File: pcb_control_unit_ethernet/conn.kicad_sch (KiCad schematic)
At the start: 18 parts, among them J10 TOF1, J11 RGB, J12 LightBarrier1, J13 LightBarrier2, J14 LightBarrier3, J15 PressureTransducer, J16 CAN, J6 USB STM32, J7 Malibotti, J8 TOF3, J9 TOF2

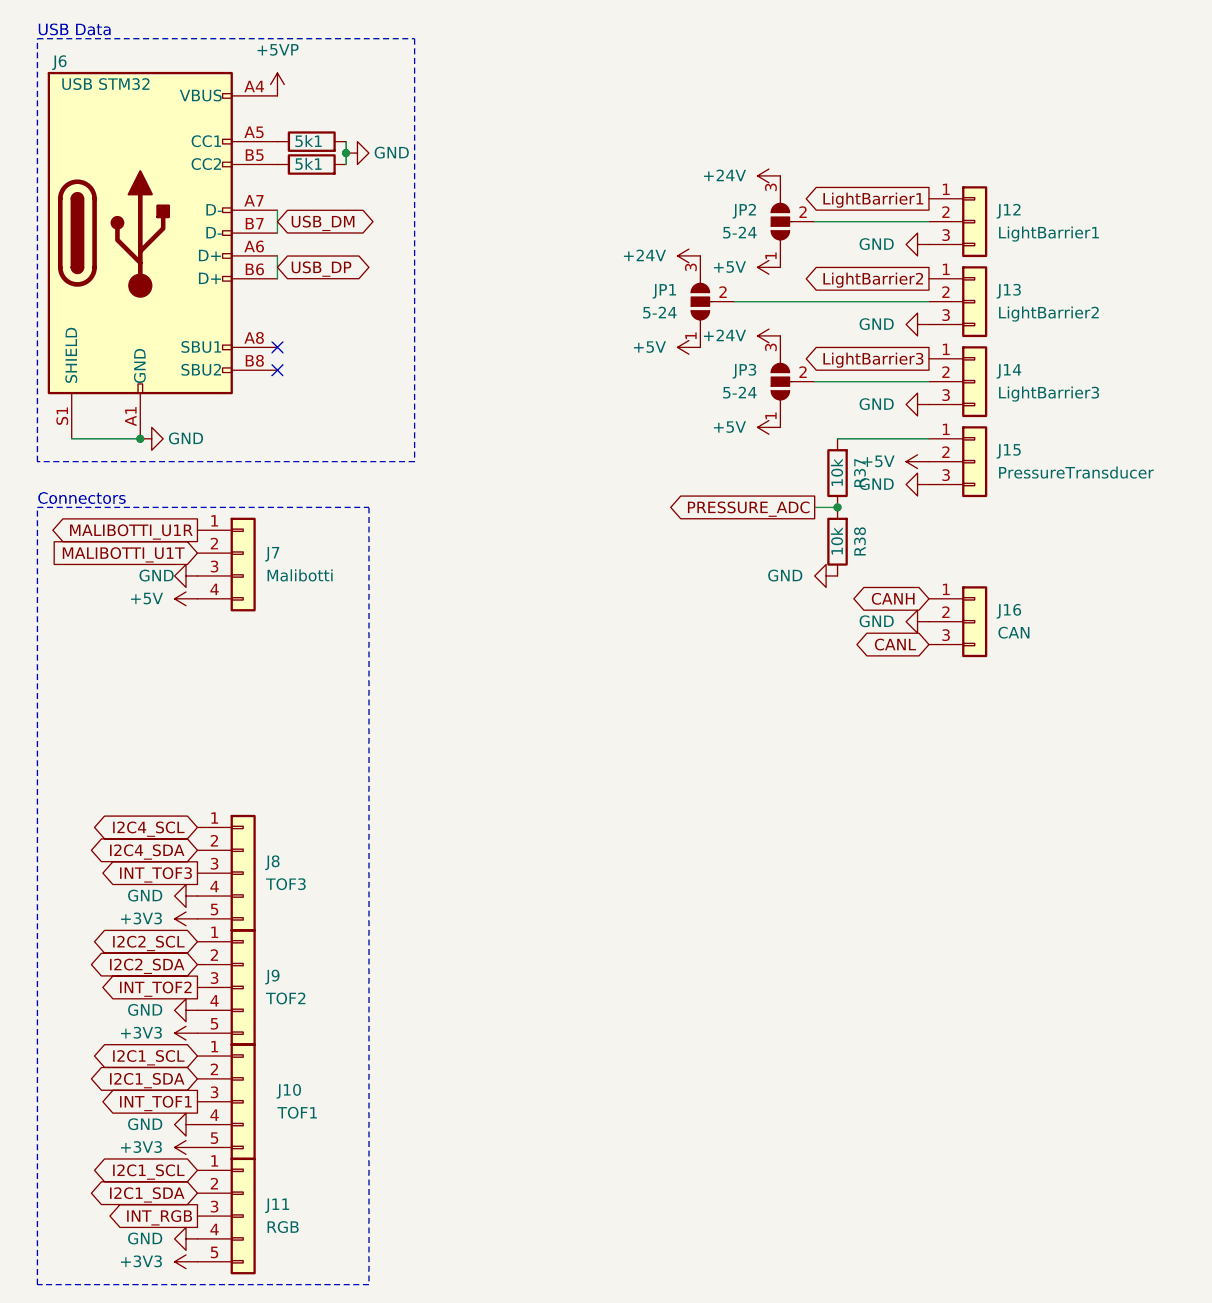
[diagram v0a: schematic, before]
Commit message: First time zero errors, but bad layout
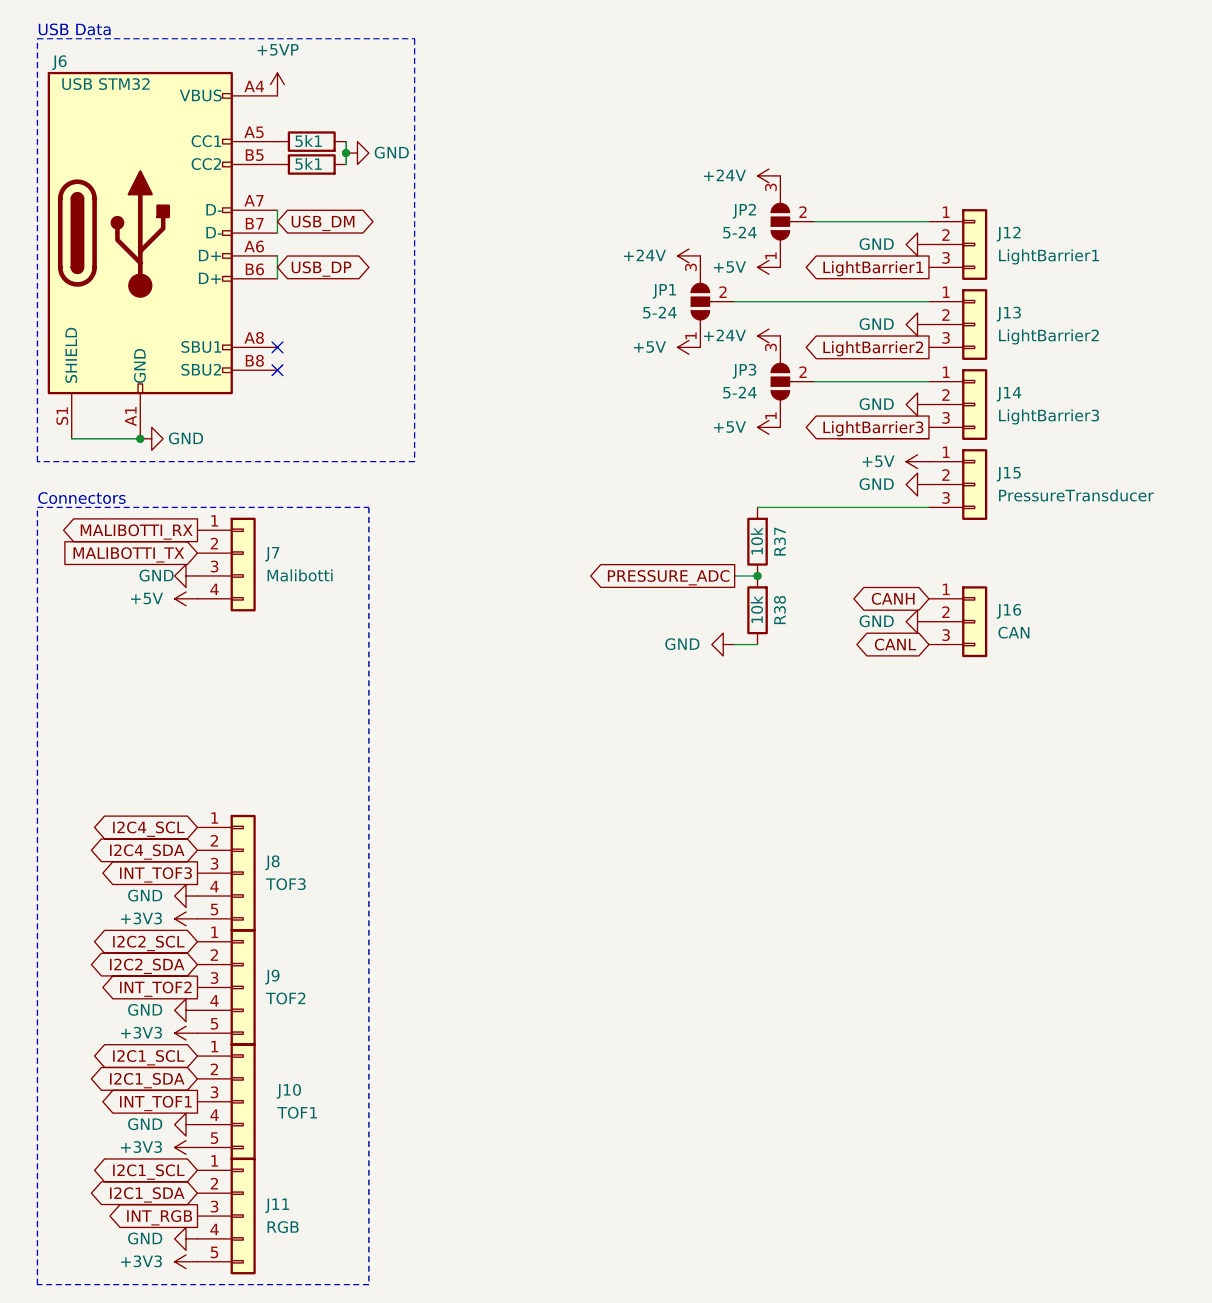
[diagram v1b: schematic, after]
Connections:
- net +5V: now also J15.1 (Pin_1); no longer J15.2 (Pin_2)
- net GND: now also J12.2 (Pin_2), J13.2 (Pin_2), J14.2 (Pin_2), J15.2 (Pin_2); no longer J12.3 (Pin_3), J13.3 (Pin_3), J14.3 (Pin_3), J15.3 (Pin_3)
- net LightBarrier1: now also J12.3 (Pin_3); no longer J12.1 (Pin_1)
- net LightBarrier2: now also J13.3 (Pin_3); no longer J13.1 (Pin_1)
- net LightBarrier3: now also J14.3 (Pin_3); no longer J14.1 (Pin_1)
- net at JP2.2 (C): now also J12.1 (Pin_1); no longer J12.2 (Pin_2)
- net at JP3.2 (C): now also J14.1 (Pin_1); no longer J14.2 (Pin_2)
- net at JP1.2 (C): now also J13.1 (Pin_1); no longer J13.2 (Pin_2)
- net at R37.2: now also J15.3 (Pin_3); no longer J15.1 (Pin_1)
- net MALIBOTTI_U1R renamed MALIBOTTI_RX
- net MALIBOTTI_U1T renamed MALIBOTTI_TX
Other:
- moved on the sheet: J12, J13, J14, J15, R37, R38
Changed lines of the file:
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@@
 	)
 	(junction
-		(at 102.87 67.31)
+		(at 93.98 74.93)
 		(diameter 0)
 		(color 0 0 0 0)
@@
 	(wire
 		(pts
-			(xy 100.33 67.31) (xy 102.87 67.31)
+			(xy 91.44 74.93) (xy 93.98 74.93)
 		)
 		(stroke
@@
 	(wire
 		(pts
+			(xy 91.44 82.55) (xy 93.98 82.55)
+		)
+		(stroke
+			(width 0)
+			(type default)
+		)
+	)
+	(wire
+		(pts
 			(xy 91.44 44.45) (xy 113.03 44.45)
 		)
@@
 		)
 	)
+	(wire
+		(pts
+			(xy 93.98 67.31) (xy 113.03 67.31)
+		)
+		(stroke
+			(width 0)
+			(type default)
+		)
+	)
 	(global_label "INT_TOF2"
 		(shape output)
@@
 	(global_label "LightBarrier3"
 		(shape output)
-		(at 113.03 50.8 180)
+		(at 113.03 58.42 180)
 		(fields_autoplaced yes)
 		(effects
@@
 		)
 		(property "Intersheetrefs" "${INTERSHEET_REFS}"
-			(at 97.7077 50.8 0)
+			(at 97.7077 58.42 0)
 			(effects
 				(font
@@
 		)
 	)
-	(global_label "MALIBOTTI_U1T"
+	(global_label "MALIBOTTI_TX"
 		(shape input)
 		(at 31.75 72.39 180)
@@
 		)
 		(property "Intersheetrefs" "${INTERSHEET_REFS}"
-			(at 14.9762 72.39 0)
+			(at 16.3067 72.39 0)
 			(effects
 				(font
@@
 		)
 	)
-	(global_label "MALIBOTTI_U1R"
+	(global_label "MALIBOTTI_RX"
 		(shape output)
 		(at 31.75 69.85 180)
@@
 		)
 		(property "Intersheetrefs" "${INTERSHEET_REFS}"
-			(at 14.6738 69.85 0)
+			(at 16.0043 69.85 0)
 			(effects
 				(font
@@
 	(global_label "LightBarrier1"
 		(shape output)
-		(at 113.03 33.02 180)
+		(at 113.03 40.64 180)
 		(fields_autoplaced yes)
 		(effects
@@
 		)
 		(property "Intersheetrefs" "${INTERSHEET_REFS}"
-			(at 97.7077 33.02 0)
+			(at 97.7077 40.64 0)
 			(effects
 				(font
@@
 	(global_label "LightBarrier2"
 		(shape output)
-		(at 113.03 41.91 180)
+		(at 113.03 49.53 180)
 		(fields_autoplaced yes)
 		(effects
@@
 		)
 		(property "Intersheetrefs" "${INTERSHEET_REFS}"
-			(at 97.7077 41.91 0)
+			(at 97.7077 49.53 0)
 			(effects
 				(font
@@
 	(global_label "PRESSURE_ADC"
 		(shape output)
-		(at 100.33 67.31 180)
+		(at 91.44 74.93 180)
 		(fields_autoplaced yes)
 		(effects
@@
 		)
 		(property "Intersheetrefs" "${INTERSHEET_REFS}"
-			(at 82.8911 67.31 0)
+			(at 74.0011 74.93 0)
 			(effects
 				(font
@@
 	(symbol
 		(lib_id "Connector_Generic:Conn_01x03")
-		(at 118.11 44.45 0)
+		(at 118.11 46.99 0)
 		(unit 1)
 		(exclude_from_sim no)
@@
 		(fields_autoplaced yes)
 		(property "Reference" "J13"
-			(at 120.65 43.1799 0)
+			(at 120.65 45.7199 0)
 			(effects
 				(font
@@
 		)
 		(property "Value" "LightBarrier2"
-			(at 120.65 45.7199 0)
+			(at 120.65 48.2599 0)
 			(effects
 				(font
@@
 		)
 		(property "Footprint" "liebler_CONN:JST_XH_B3B-XH-A_1x03_P2.50mm_Vertical_smaller"
-			(at 118.11 44.45 0)
+			(at 118.11 46.99 0)
 			(effects
 				(font
@@
 		)
 		(property "Datasheet" "~"
-			(at 118.11 44.45 0)
+			(at 118.11 46.99 0)
 			(effects
 				(font
@@
 		)
 		(property "Description" "Generic connector, single row, 01x03, script generated (kicad-library-utils/schlib/autogen/connector/)"
-			(at 118.11 44.45 0)
+			(at 118.11 46.99 0)
 			(effects
 				(font
@@
 	(symbol
 		(lib_id "Device:R")
-		(at 102.87 71.12 180)
+		(at 93.98 78.74 180)
 		(unit 1)
 		(exclude_from_sim no)
@@
 		(dnp no)
 		(property "Reference" "R38"
-			(at 105.41 71.12 90)
+			(at 96.52 78.74 90)
 			(effects
 				(font
@@
 		)
 		(property "Value" "10k"
-			(at 102.87 71.12 90)
+			(at 93.98 78.74 90)
 			(effects
 				(font
@@
 		)
 		(property "Footprint" "Resistor_SMD:R_0402_1005Metric"
-			(at 104.648 71.12 90)
+			(at 95.758 78.74 90)
 			(effects
 				(font
@@
 		)
 		(property "Datasheet" "~"
-			(at 102.87 71.12 0)
+			(at 93.98 78.74 0)
 			(effects
 				(font
@@
 		)
 		(property "Description" ""
-			(at 102.87 71.12 0)
+			(at 93.98 78.74 0)
 			(effects
 				(font
@@
 		)
 		(property "MPN" "0201WMF1002TEE"
-			(at 102.87 71.12 0)
+			(at 93.98 78.74 0)
 			(effects
 				(font
@@
 		)
 		(property "Manufacturer" "UNI-ROYAL(Uniroyal Elec)"
-			(at 102.87 71.12 0)
+			(at 93.98 78.74 0)
 			(effects
 				(font
@@
 	(symbol
 		(lib_id "Device:R")
-		(at 102.87 63.5 180)
+		(at 93.98 71.12 180)
 		(unit 1)
 		(exclude_from_sim no)
@@
 		(dnp no)
 		(property "Reference" "R37"
-			(at 105.41 63.5 90)
+			(at 96.52 71.12 90)
 			(effects
 				(font
@@
 		)
 		(property "Value" "10k"
-			(at 102.87 63.5 90)
+			(at 93.98 71.12 90)
 			(effects
 				(font
@@
 		)
 		(property "Footprint" "Resistor_SMD:R_0402_1005Metric"
-			(at 104.648 63.5 90)
+			(at 95.758 71.12 90)
 			(effects
 				(font
@@
 		)
 		(property "Datasheet" "~"
-			(at 102.87 63.5 0)
+			(at 93.98 71.12 0)
 			(effects
 				(font
@@
 		)
 		(property "Description" ""
-			(at 102.87 63.5 0)
+			(at 93.98 71.12 0)
 			(effects
 				(font
@@
 		)
 		(property "MPN" "0201WMF1002TEE"
-			(at 102.87 63.5 0)
+			(at 93.98 71.12 0)
 			(effects
 				(font
@@
 		)
 		(property "Manufacturer" "UNI-ROYAL(Uniroyal Elec)"
-			(at 102.87 63.5 0)
+			(at 93.98 71.12 0)
 			(effects
 				(font
@@
 	(symbol
 		(lib_id "power:GND")
-		(at 102.87 74.93 270)
+		(at 91.44 82.55 270)
 		(unit 1)
 		(exclude_from_sim no)
@@
 		(fields_autoplaced yes)
 		(property "Reference" "#PWR086"
-			(at 96.52 74.93 0)
+			(at 85.09 82.55 0)
 			(effects
 				(font
@@
 		)
 		(property "Value" "GND"
-			(at 99.06 74.9299 90)
+			(at 87.63 82.5499 90)
 			(effects
 				(font
@@
 		)
 		(property "Footprint" ""
-			(at 102.87 74.93 0)
+			(at 91.44 82.55 0)
 			(effects
 				(font
@@
 		)
 		(property "Datasheet" ""
-			(at 102.87 74.93 0)
+			(at 91.44 82.55 0)
 			(effects
 				(font
@@
 		)
 		(property "Description" "Power symbol creates a global label with name \"GND\" , ground"
-			(at 102.87 74.93 0)
+			(at 91.44 82.55 0)
 			(effects
 				(font
@@
 	(symbol
 		(lib_id "Connector_Generic:Conn_01x03")
-		(at 118.11 53.34 0)
+		(at 118.11 55.88 0)
 		(unit 1)
 		(exclude_from_sim no)
@@
 		(fields_autoplaced yes)
 		(property "Reference" "J14"
-			(at 120.65 52.0699 0)
+			(at 120.65 54.6099 0)
 			(effects
 				(font
@@
 		)
 		(property "Value" "LightBarrier3"
-			(at 120.65 54.6099 0)
+			(at 120.65 57.1499 0)
 			(effects
 				(font
@@
 		)
 		(property "Footprint" "liebler_CONN:JST_XH_B3B-XH-A_1x03_P2.50mm_Vertical_smaller"
-			(at 118.11 53.34 0)
+			(at 118.11 55.88 0)
 			(effects
 				(font
@@
 		)
 		(property "Datasheet" "~"
-			(at 118.11 53.34 0)
+			(at 118.11 55.88 0)
 			(effects
 				(font
@@
 		)
 		(property "Description" "Generic connector, single row, 01x03, script generated (kicad-library-utils/schlib/autogen/connector/)"
-			(at 118.11 53.34 0)
+			(at 118.11 55.88 0)
 			(effects
 				(font
@@
 	(symbol
 		(lib_id "Connector_Generic:Conn_01x03")
-		(at 118.11 35.56 0)
+		(at 118.11 38.1 0)
 		(unit 1)
 		(exclude_from_sim no)
@@
 		(fields_autoplaced yes)
 		(property "Reference" "J12"
-			(at 120.65 34.2899 0)
+			(at 120.65 36.8299 0)
 			(effects
 				(font
@@
 		)
 		(property "Value" "LightBarrier1"
-			(at 120.65 36.8299 0)
+			(at 120.65 39.3699 0)
 			(effects
 				(font
@@
 		)
 		(property "Footprint" "liebler_CONN:JST_XH_B3B-XH-A_1x03_P2.50mm_Vertical_smaller"
-			(at 118.11 35.56 0)
+			(at 118.11 38.1 0)
 			(effects
 				(font
@@
 		)
 		(property "Datasheet" "~"
-			(at 118.11 35.56 0)
+			(at 118.11 38.1 0)
 			(effects
 				(font
@@
 		)
 		(property "Description" "Generic connector, single row, 01x03, script generated (kicad-library-utils/schlib/autogen/connector/)"
-			(at 118.11 35.56 0)
+			(at 118.11 38.1 0)
 			(effects
 				(font
@@
 	(symbol
 		(lib_id "Connector_Generic:Conn_01x03")
-		(at 118.11 62.23 0)
+		(at 118.11 64.77 0)
 		(unit 1)
 		(exclude_from_sim no)
@@
 		(fields_autoplaced yes)
 		(property "Reference" "J15"
-			(at 120.65 60.9599 0)
+			(at 120.65 63.4999 0)
 			(effects
 				(font
@@
 		)
 		(property "Value" "PressureTransducer"
-			(at 120.65 63.4999 0)
+			(at 120.65 66.0399 0)
 			(effects
 				(font
@@
 		)
 		(property "Footprint" "liebler_CONN:JST_XH_B3B-XH-A_1x03_P2.50mm_Vertical_smaller"
-			(at 118.11 62.23 0)
+			(at 118.11 64.77 0)
 			(effects
 				(font
@@
 		)
 		(property "Datasheet" "~"
-			(at 118.11 62.23 0)
+			(at 118.11 64.77 0)
 			(effects
 				(font
@@
 		)
 		(property "Description" "Generic connector, single row, 01x03, script generated (kicad-library-utils/schlib/autogen/connector/)"
-			(at 118.11 62.23 0)
+			(at 118.11 64.77 0)
 			(effects
 				(font

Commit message: WIP
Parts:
- added J24: WS2812_CH1, liebler_CONN:JST_XH_B3B-XH-A_1x03_P2.50mm_Vertical_smaller, symbol Connector_Generic:Conn_01x03
- added J25: WS2812_CH2, liebler_CONN:JST_XH_B3B-XH-A_1x03_P2.50mm_Vertical_smaller, symbol Connector_Generic:Conn_01x03
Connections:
- net +5V: now also J24.1 (Pin_1), J25.1 (Pin_1)
- net GND: now also J24.2 (Pin_2), J25.2 (Pin_2)
- new net WS2812_CH1: J24.3 (Pin_3)
- new net WS2812_CH2: J25.3 (Pin_3)
